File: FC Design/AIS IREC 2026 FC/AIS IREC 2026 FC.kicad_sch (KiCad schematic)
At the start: 47 parts, among them IC1 ADXL314WBCPZ-RL, IC2 MT29F8G08ABACAWP-IT_C_TR, J1 USB4216-03-A, J2 EBAA-02-C, J3 Conn_01x08, J4 EBAA-02-C, J5 EBAA-02-C, Q1 MMBT3906-TP, U1 STM32F205VBTx, U2 KC2520Z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

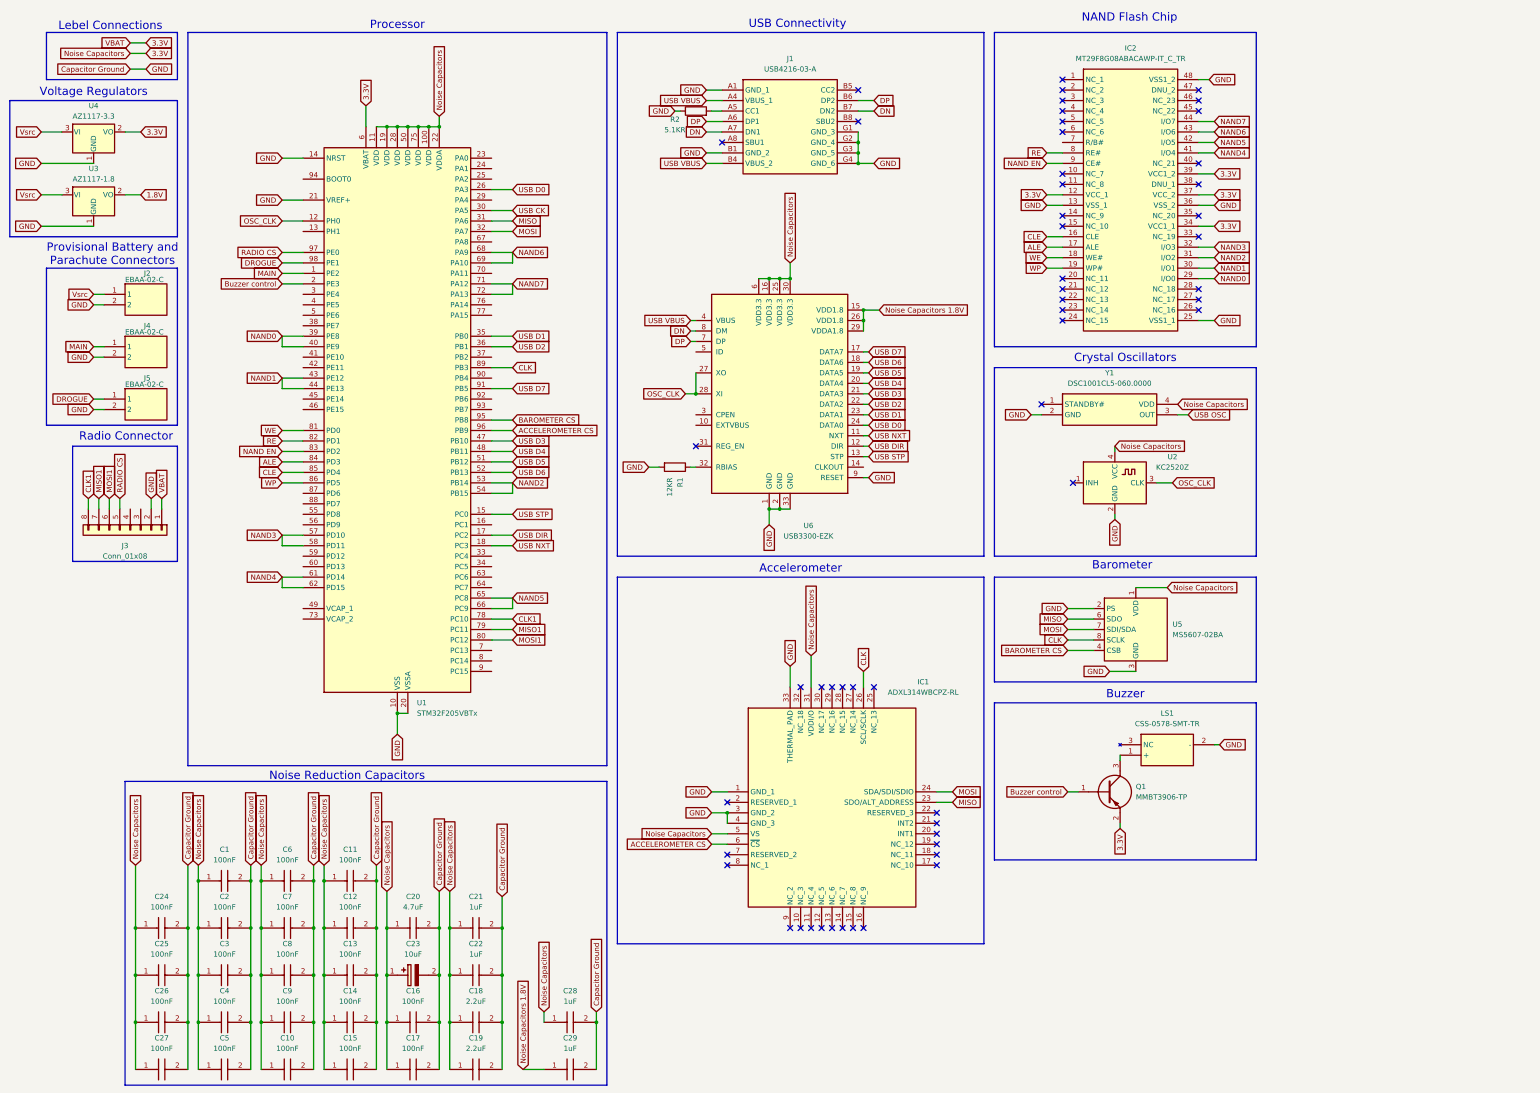
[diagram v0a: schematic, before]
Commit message: Added transistors to schematic
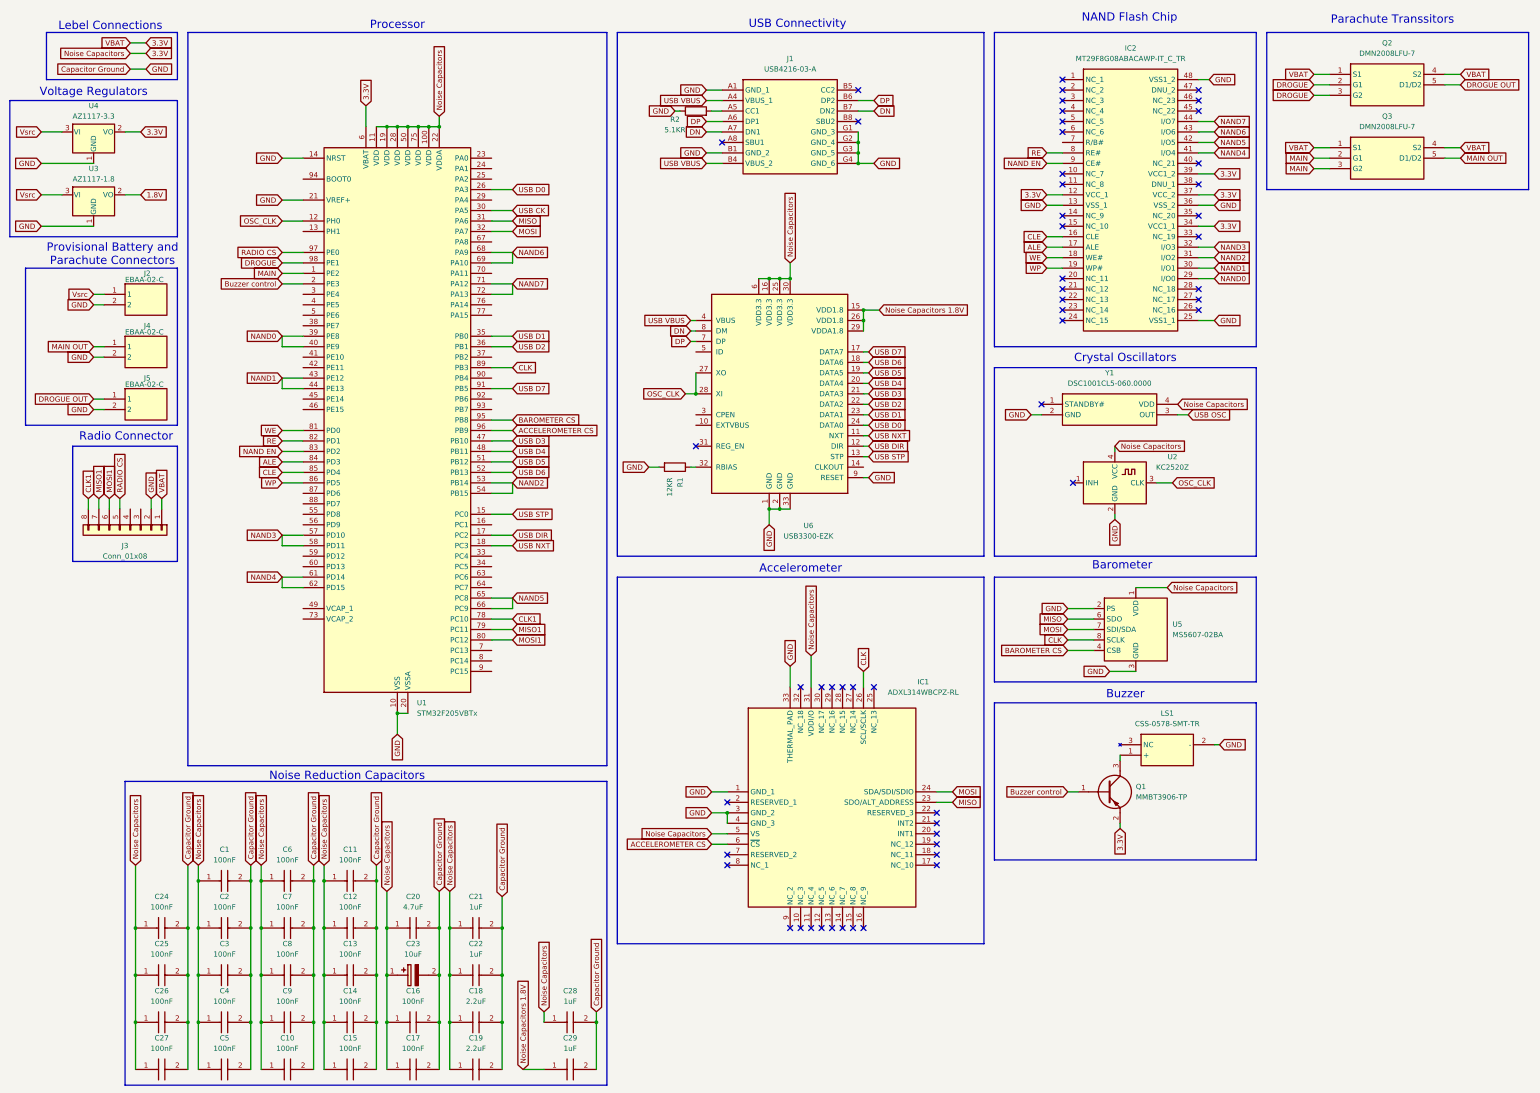
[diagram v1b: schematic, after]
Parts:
- added Q2, Q3: DMN2008LFU-7, DMN2008LFU7, symbol SamacSys_Parts:DMN2008LFU-7
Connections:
- net 3.3V: now also Q2.1 (S1), Q2.4 (S2), Q3.1 (S1), Q3.4 (S2)
- net DROGUE: now also Q2.2 (G1), Q2.3 (G2); no longer J5.1
- net MAIN: now also Q3.2 (G1), Q3.3 (G2); no longer J4.1
- new net DROGUE OUT: J5.1, Q2.5 (D1/D2)
- new net MAIN OUT: J4.1, Q3.5 (D1/D2)
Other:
- note added: "Parachute Transsitors"

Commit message: Altered FC design and setup on Cube IDE for flashing
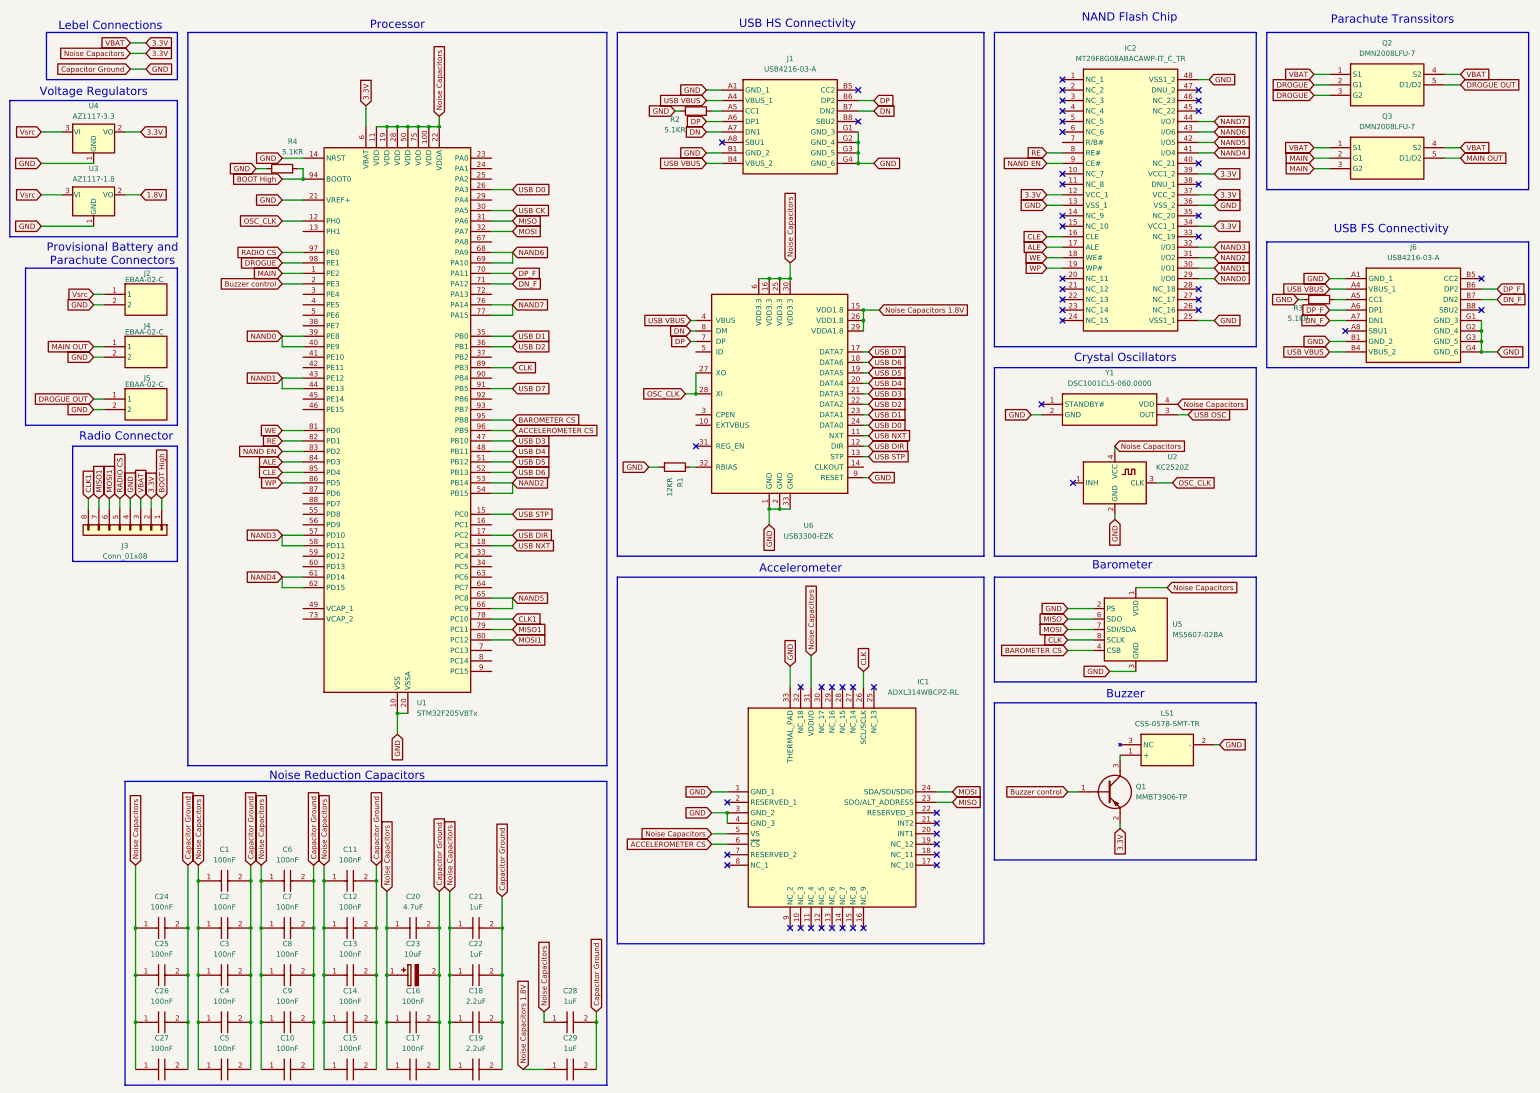
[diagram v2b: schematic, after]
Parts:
- added J6: USB4216-03-A, SamacSys_Parts:USB421603A, symbol SamacSys_Parts:USB4216-03-A
- added R3, R4: 5.1KR, Resistor_SMD:R_0201_0603Metric, symbol Device:R
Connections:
- net 3.3V: now also J3.2 (Pin_2), J3.3 (Pin_3); no longer J3.1 (Pin_1)
- net Capacitor Ground: now also J3.4 (Pin_4), J6.A1 (GND_1), J6.B1 (GND_2), J6.G1 (GND_3), J6.G2 (GND_4), J6.G3 (GND_5), J6.G4 (GND_6), R3.1, R4.1; no longer J3.2 (Pin_2)
- net NAND7: now also U1.76 (PA14), U1.77 (PA15); no longer U1.71 (PA12), U1.72 (PA13)
- net USB VBUS: now also J6.A4 (VBUS_1), J6.B4 (VBUS_2)
- net DP_F: now reaches U1.70 (PA11)
- net DP_F: now also J6.A6 (DP1), J6.B6 (DP2)
- net BOOT High: now reaches U1.94 (BOOT0)
- net BOOT High: now also J3.1 (Pin_1), R4.2
- new net: J6.A5 (CC1), R3.2
- new net DN_F: J6.A7 (DN1), J6.B7 (DN2), U1.71 (PA12)
- no-connect marks 54 -> 57
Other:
- note added: "USB FS Connectivity"
- note added: "USB HS Connectivity"
- note removed: "USB Connectivity"

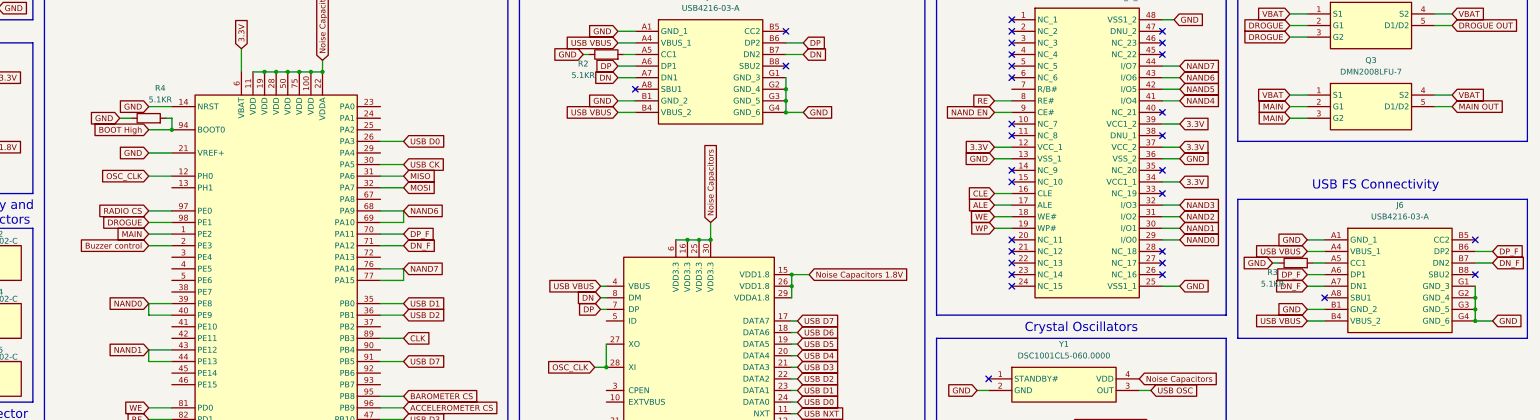
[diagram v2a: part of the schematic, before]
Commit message: Updates to wiring to help with flashing of microprocessor
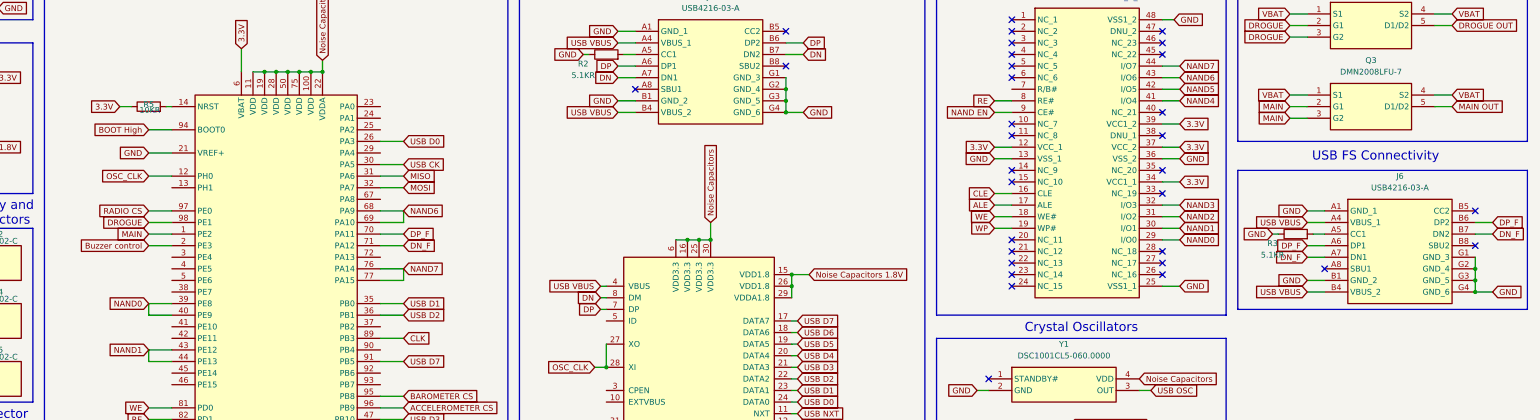
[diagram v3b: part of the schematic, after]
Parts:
- removed R4: 5.1KR, Resistor_SMD:R_0201_0603Metric, symbol Device:R
- added R5: 10KR, Resistor_SMD:R_0201_0603Metric, symbol Device:R
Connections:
- net 3.3V: now also R5.1
- net Capacitor Ground: no longer U1.14 (NRST)
- new net: R5.2, U1.14 (NRST)
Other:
- moved on the sheet: J6, R3
